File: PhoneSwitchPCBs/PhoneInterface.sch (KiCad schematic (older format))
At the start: 51 parts

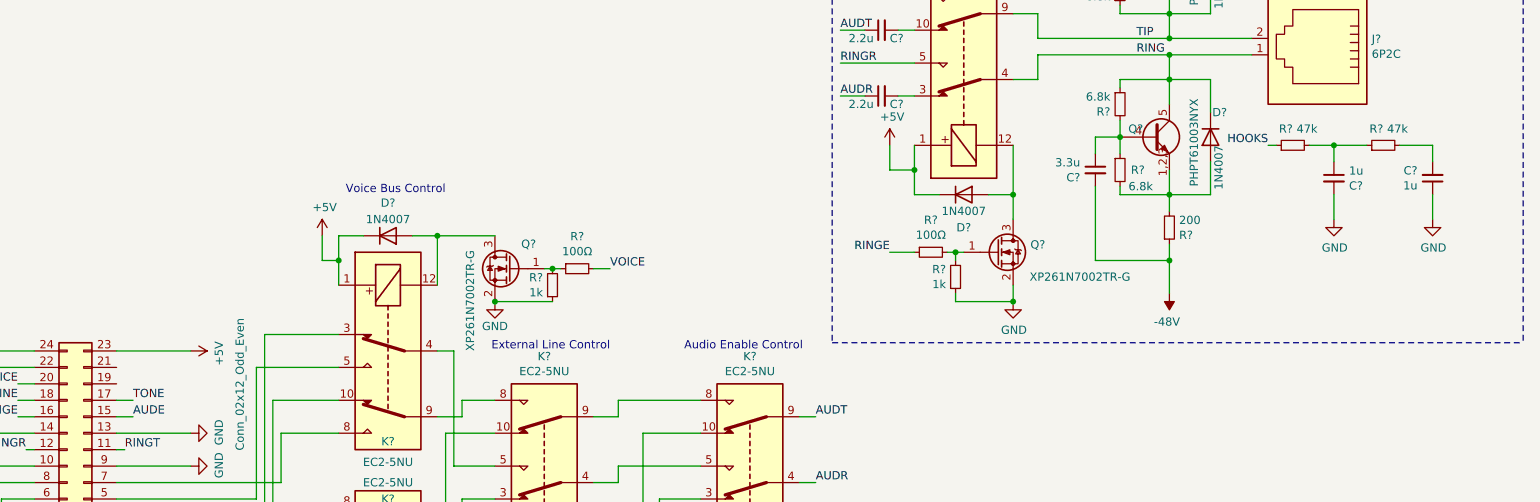
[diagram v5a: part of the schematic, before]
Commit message: Progress on schematic, switch to using software filtering
Clean up notes regarding only needing a single Schmitt trigger for software-based filtering of ring trip.  Remove the unneeded switch IC from notes as well as the schematic, and remove the filter.
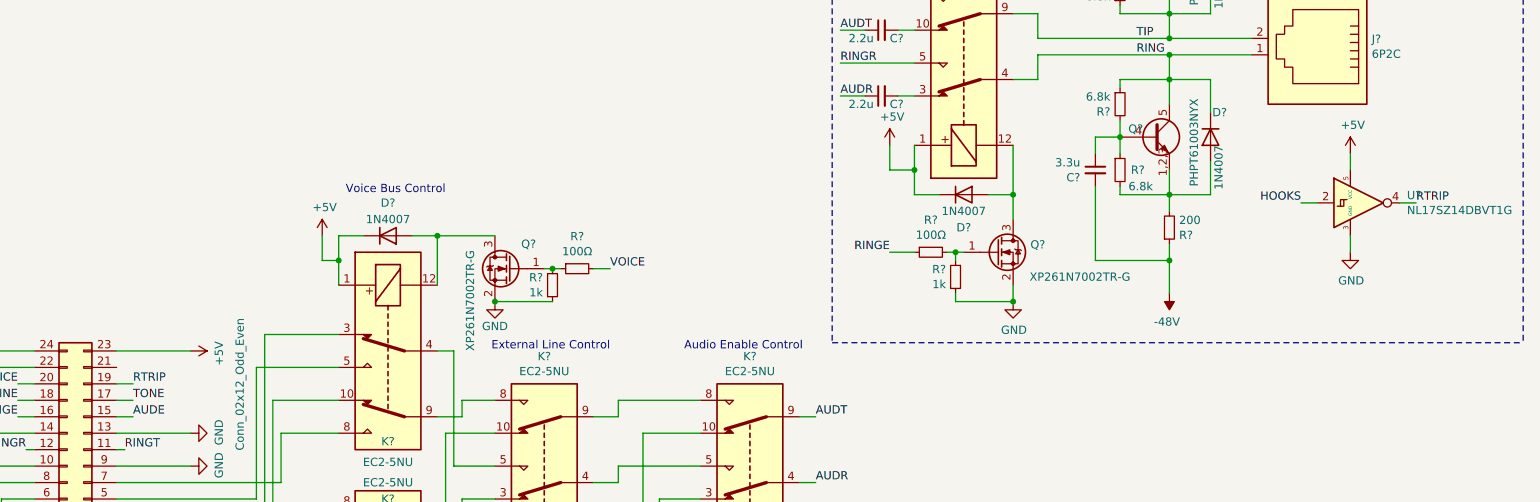
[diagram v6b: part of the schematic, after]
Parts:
- removed C? (x2): 1u, symbol Device:C_Small
- removed R? (x2): 47k, symbol Device:R_Small
- added U?: NL17SZ14DBVT1G, Package_TO_SOT_SMD:SOT-23-5, symbol PhoneInterfaceParts:NL17SZ14DBVT1G
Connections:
- net +5V: now also U?.5 (VCC)
- net GND: now also U?.3 (GND)
- net HOOKS: now also U?.2
- net RTRIP: now reaches J?.19 (Pin_19)
- net RTRIP: now also U?.4
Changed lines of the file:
@@
 Wire Notes Line
 	6050 4600 10250 4600
-$Comp
-L Device:R_Small R?
-U 1 1 618AB787
-P 8850 3400
-F 0 "R?" V 8950 3400 50  0000 L CNN
-F 1 "47k" V 8950 3250 50  0000 L CNN
-F 2 "" H 8850 3400 50  0001 C CNN
-F 3 "~" H 8850 3400 50  0001 C CNN
-	1    8850 3400
-	0    -1   -1   0
-$EndComp
-$Comp
-L Device:C_Small C?
-U 1 1 618ABAFE
-P 9100 3600
-F 0 "C?" H 9008 3554 50  0000 R CNN
-F 1 "1u" H 9008 3645 50  0000 R CNN
-F 2 "" H 9100 3600 50  0001 C CNN
-F 3 "~" H 9100 3600 50  0001 C CNN
-	1    9100 3600
-	-1   0    0    -1
-$EndComp
-$Comp
-L power:GND #PWR?
-U 1 1 618BB6CA
-P 9100 3850
-F 0 "#PWR?" H 9100 3600 50  0001 C CNN
-F 1 "GND" H 9105 3677 50  0000 C CNN
-F 2 "" H 9100 3850 50  0001 C CNN
-F 3 "" H 9100 3850 50  0001 C CNN
-	1    9100 3850
-	1    0    0    -1
-$EndComp
-$Comp
-L Device:R_Small R?
-U 1 1 618CAA0B
-P 9400 3400
-F 0 "R?" V 9500 3400 50  0000 L CNN
-F 1 "47k" V 9500 3250 50  0000 L CNN
-F 2 "" H 9400 3400 50  0001 C CNN
-F 3 "~" H 9400 3400 50  0001 C CNN
-	1    9400 3400
-	0    -1   -1   0
-$EndComp
-$Comp
-L Device:C_Small C?
-U 1 1 61907E2B
-P 9700 3600
-F 0 "C?" H 9608 3554 50  0000 R CNN
-F 1 "1u" H 9608 3645 50  0000 R CNN
-F 2 "" H 9700 3600 50  0001 C CNN
-F 3 "~" H 9700 3600 50  0001 C CNN
-	1    9700 3600
-	1    0    0    1
-$EndComp
 Wire Wire Line
 	9400 1500 9450 1500
@@
 Text Label 9450 1500 0    50   ~ 0
 HOOKS
-Text Label 8700 3400 2    50   ~ 0
-HOOKS
 Wire Wire Line
-	9100 3500 9100 3400
-Wire Wire Line
-	9100 3400 8950 3400
-Wire Wire Line
-	9100 3850 9100 3700
-Wire Wire Line
-	9300 3400 9100 3400
-Connection ~ 9100 3400
-Wire Wire Line
-	9700 3500 9700 3400
-Wire Wire Line
-	9700 3400 9500 3400
+	1700 4850 1800 4850
+Text Label 1800 4850 0    50   ~ 0
+RTRIP
+$Comp
+L PhoneInterfaceParts:NL17SZ14DBVT1G U?
+U 1 1 61015085
+P 9200 3750
+F 0 "U?" H 9544 3796 50  0000 L CNN
+F 1 "NL17SZ14DBVT1G" H 9544 3705 50  0000 L CNN
+F 2 "Package_TO_SOT_SMD:SOT-23-5" H 9200 3500 50  0001 C CNN
+F 3 "https://www.mouser.com/datasheet/2/308/1/NL17SZ14_D-2318143.pdf" H 9200 3750 50  0001 C CNN
+	1    9200 3750
+	1    0    0    -1
+$EndComp
+$Comp
+L power:+5V #PWR?
+U 1 1 61015DE5
+P 9200 3450
+F 0 "#PWR?" H 9200 3300 50  0001 C CNN
+F 1 "+5V" H 9215 3623 50  0000 C CNN
+F 2 "" H 9200 3450 50  0001 C CNN
+F 3 "" H 9200 3450 50  0001 C CNN
+	1    9200 3450
+	1    0    0    -1
+$EndComp
 $Comp
 L power:GND #PWR?
-U 1 1 619B703E
-P 9700 3850
-F 0 "#PWR?" H 9700 3600 50  0001 C CNN
-F 1 "GND" H 9705 3677 50  0000 C CNN
-F 2 "" H 9700 3850 50  0001 C CNN
-F 3 "" H 9700 3850 50  0001 C CNN
-	1    9700 3850
+U 1 1 610166B4
+P 9200 4050
+F 0 "#PWR?" H 9200 3800 50  0001 C CNN
+F 1 "GND" H 9205 3877 50  0000 C CNN
+F 2 "" H 9200 4050 50  0001 C CNN
+F 3 "" H 9200 4050 50  0001 C CNN
+	1    9200 4050
 	1    0    0    -1
 $EndComp
 Wire Wire Line
-	9700 3850 9700 3700
+	9200 3550 9200 3450
 Wire Wire Line
-	8700 3400 8750 3400
+	9200 3950 9200 4050
+Text Label 8900 3750 2    50   ~ 0
+HOOKS
+Wire Wire Line
+	9000 3750 8900 3750
+Wire Wire Line
+	9500 3750 9600 3750
+Text Label 9600 3750 0    50   ~ 0
+RTRIP
 $EndSCHEMATC

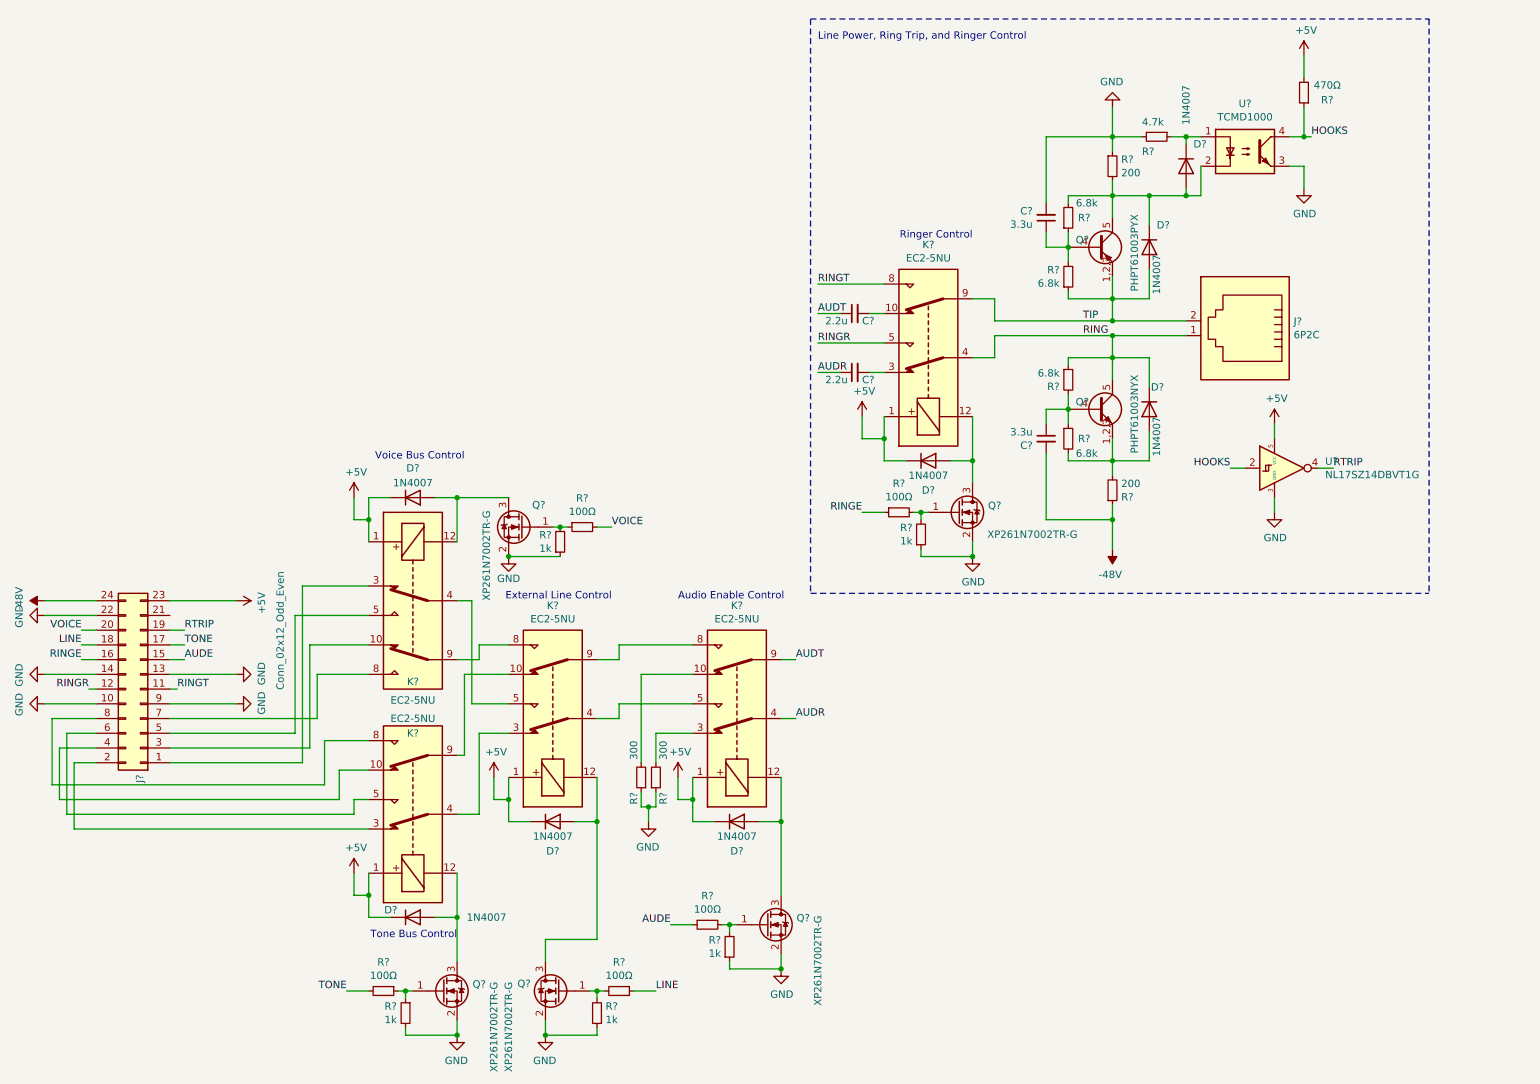
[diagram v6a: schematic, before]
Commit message: Update notes, change schematic to use 3.3 volt IO in addition to more progress
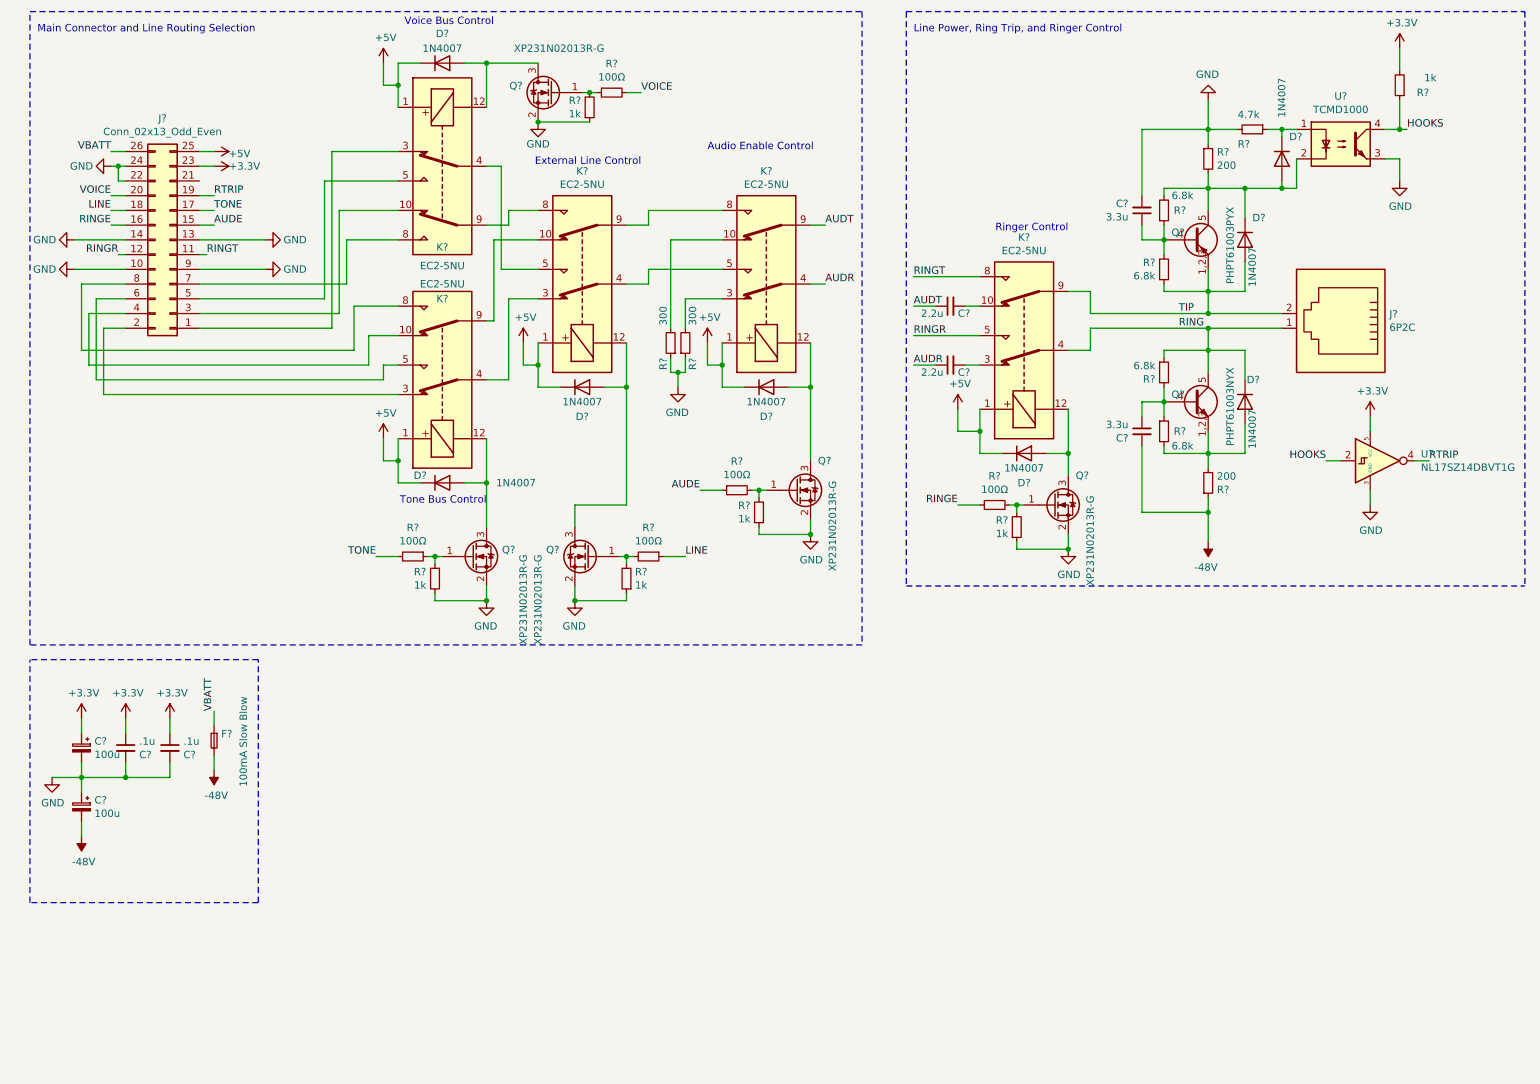
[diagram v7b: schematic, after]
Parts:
- removed J?: Conn_02x12_Odd_Even, symbol Connector_Generic:Conn_02x12_Odd_Even
- removed Q? (x5): XP261N7002TR-G, Package_TO_SOT_SMD:SOT-23, symbol PhoneInterfaceParts:XP261N7002TR-G
- added C? (x2): 100u, symbol Device:CP_Small
- added C? (x2): .1u, symbol Device:C_Small
- added F?: 100mA Slow Blow, symbol Device:Fuse_Small
- added J?: Conn_02x13_Odd_Even, symbol Connector_Generic:Conn_02x13_Odd_Even
- added Q? (x5): XP231N02013R-G, Package_TO_SOT_SMD:SOT-323_SC-70_Handsoldering, symbol PhoneInterfaceParts:XP231N02013R-G
- R?: value 470Ω -> 1k
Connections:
- net +5V: now also J?.25 (Pin_25); no longer R?.2, U?.5 (VCC)
- net -48V: now also C?.2, F?.2
- net AUDE: now also J?.15 (Pin_15)
- net GND: now also C?.1, C?.2, C?.2, C?.2, J?.10 (Pin_10), J?.13 (Pin_13), J?.14 (Pin_14), J?.22 (Pin_22), J?.24 (Pin_24), J?.9 (Pin_9), Q?.2 (S), Q?.2 (S), Q?.2 (S), Q?.2 (S), Q?.2 (S)
- net LINE: now also J?.18 (Pin_18)
- net RINGE: now also J?.16 (Pin_16)
- net RINGR: now also J?.12 (Pin_12)
- net RINGT: now also J?.11 (Pin_11)
- net RTRIP: now also J?.19 (Pin_19)
- net TONE: now also J?.17 (Pin_17)
- net VOICE: now also J?.20 (Pin_20)
- net at D?.2 (A), K?.12: now also Q?.3 (D) (x5)
- net at K?.10: now also J?.3 (Pin_3)
- net at K?.3: now also J?.1 (Pin_1)
- net at K?.5: now also J?.5 (Pin_5)
- net at K?.8: now also J?.7 (Pin_7)
- net at K?.10: now also J?.4 (Pin_4)
- net at K?.3: now also J?.2 (Pin_2)
- net at K?.5: now also J?.6 (Pin_6)
- net at K?.8: now also J?.8 (Pin_8)
- net at R?.2, R?.2: now also Q?.1 (G) (x3)
- net at R?.1, R?.1: now also Q?.1 (G)
- net at R?.1, R?.2: now also Q?.1 (G)
- new net +3V3: C?.1, C?.1, C?.1, J?.23 (Pin_23), R?.2, U?.5 (VCC)
- new net VBATT: F?.1, J?.26 (Pin_26)
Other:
- note added: "Main Connector and Line Routing Selection"
- moved on the sheet: C?, D?, J?, K?, Q?, R?, U?

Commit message: Finalize non-interchangeable station/trunk modules, mostly finish schematic
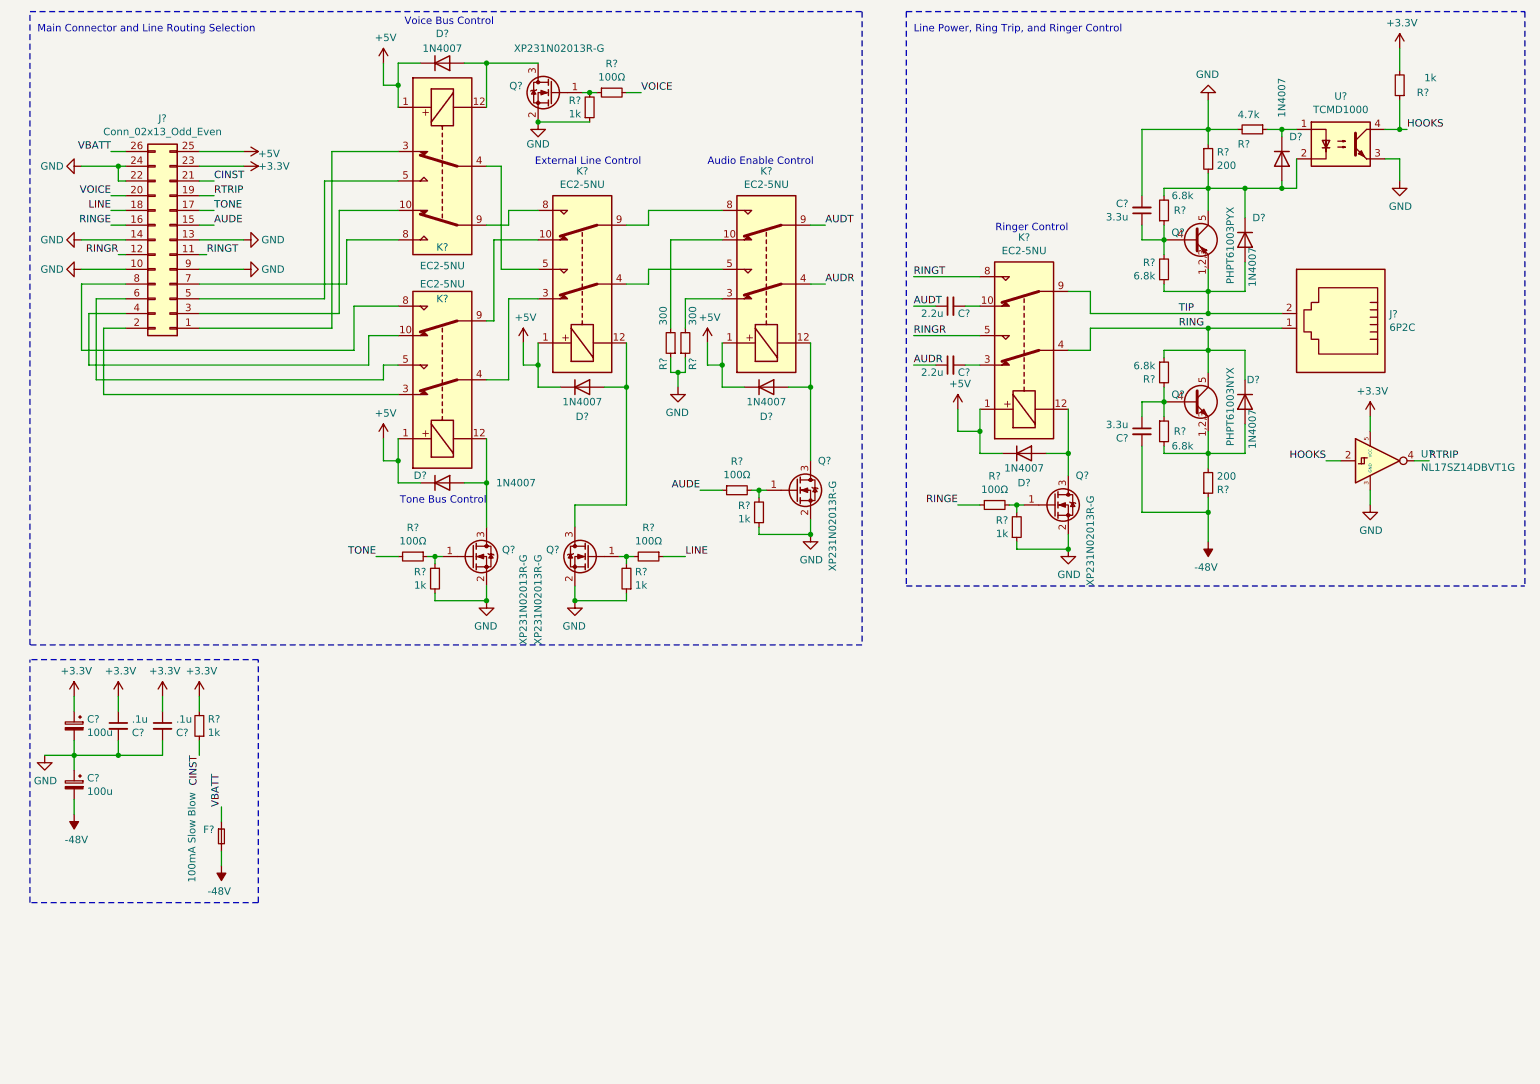
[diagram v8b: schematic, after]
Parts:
- added R?: 1k, symbol Device:R_Small
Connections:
- net +3V3: now also R?.2
- net CINST: now reaches J?.21 (Pin_21)
- net CINST: now also R?.1
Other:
- moved on the sheet: C?, F?
